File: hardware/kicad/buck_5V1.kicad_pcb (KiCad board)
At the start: 2 copper layers, 42.2 x 57.9 mm, 23 parts, among them J1 V12_IN, J2 V5_OUT, U1 LMZ23610TZ/NOPB

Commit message: docs: added pcb export - buck_5V1
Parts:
- moved J2 5.47 mm to (126.9, 96.4), turned to 180 degrees
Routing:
- net /PGND: track 13.6 -> 44.2 mm, vias 0 -> 11
- net /V12_IN: track 0.00 -> 1.27 mm
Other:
- board text added: "+"
- board text added: "-"
- board text added: "12V"
- board text added: "5V"

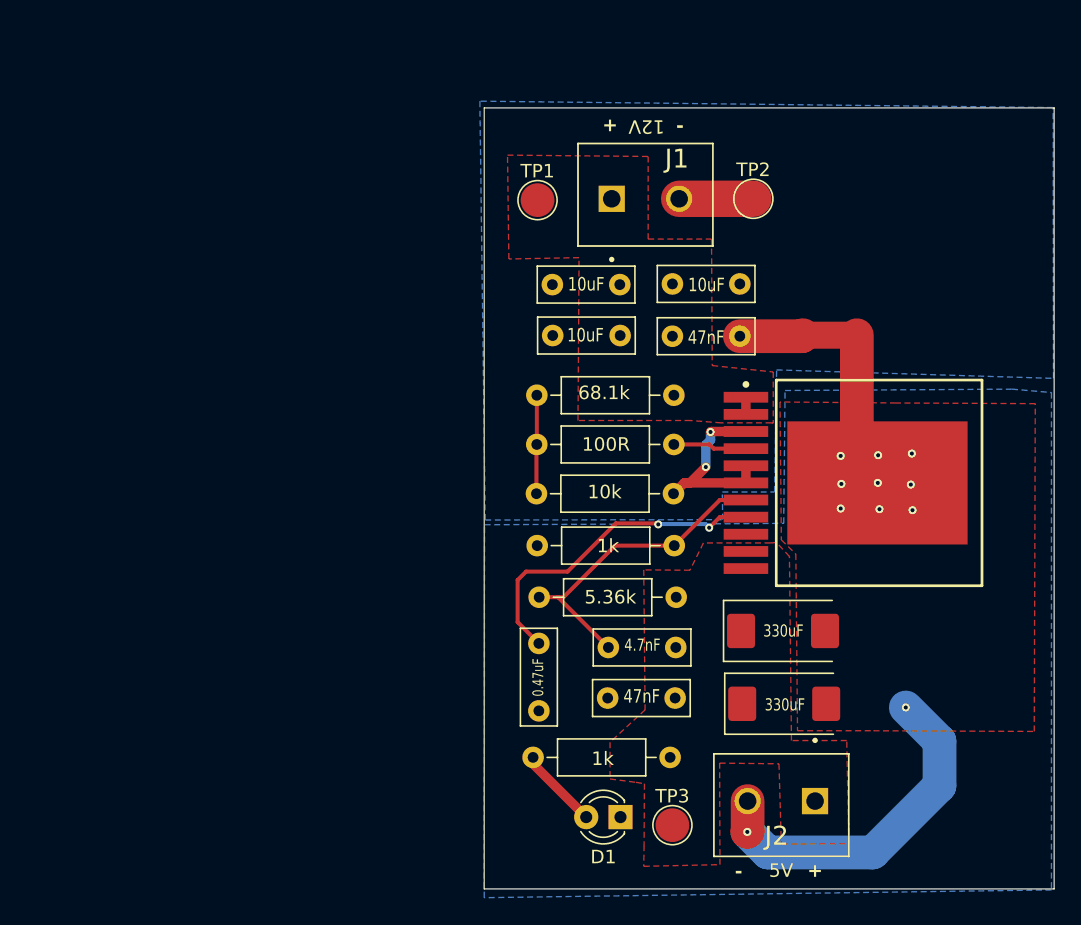
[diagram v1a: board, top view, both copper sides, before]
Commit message: fix: package change & pcb comp placement - buck5V1
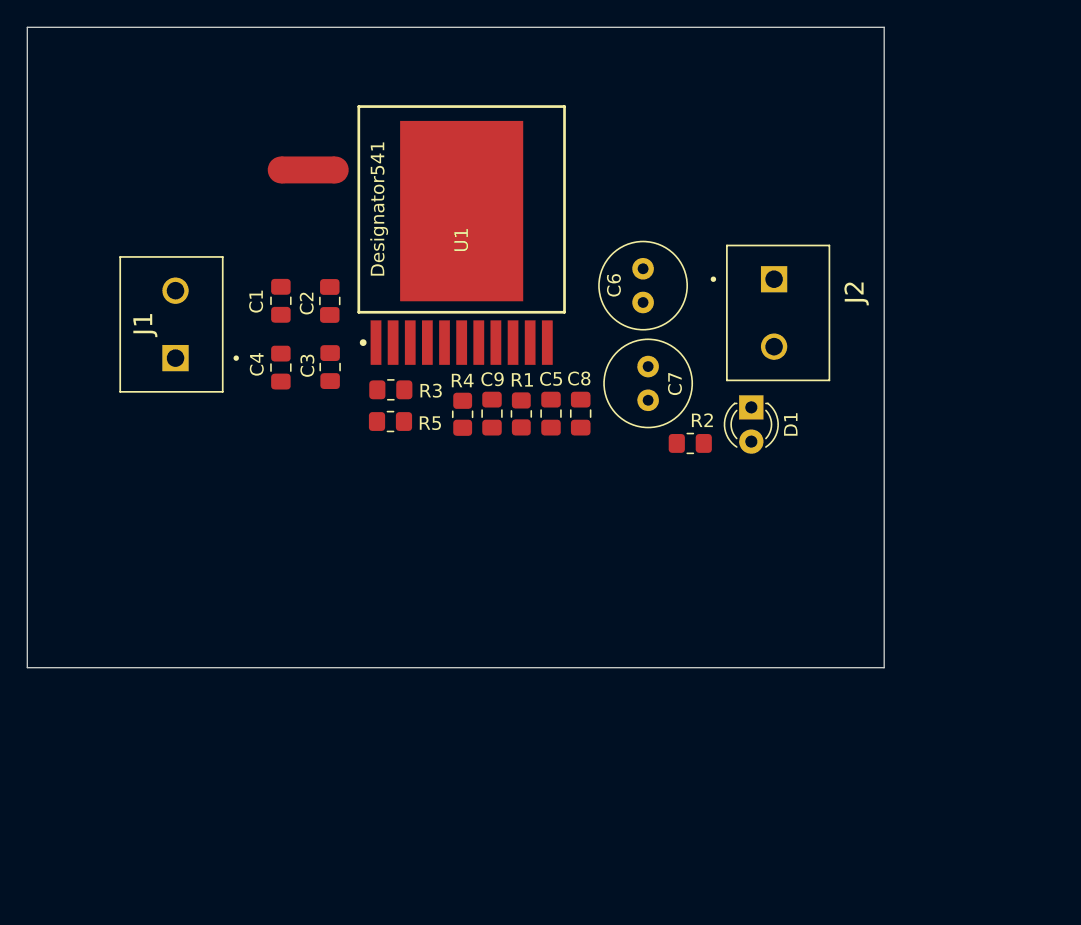
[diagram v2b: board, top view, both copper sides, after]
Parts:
- removed R6: 1k, Resistor_THT:R_Axial_DIN0207_L6.3mm_D2.5mm_P10.16mm_Horizontal
- removed TP1: V12_IN, TestPoint:TestPoint_Pad_D2.5mm
- removed TP2: GND, TestPoint:TestPoint_Pad_D2.5mm
- removed TP3: V5, TestPoint:TestPoint_Pad_D2.5mm
- C1, C2, C3, C5, C8: footprint Capacitor_THT:C_Disc_D7.0mm_W2.5mm_P5.00mm -> Capacitor_SMD:C_0805_2012Metric_Pad1.18x1.45mm_HandSolder
- C4: value 0.47uF -> 47nF; footprint Capacitor_THT:C_Disc_D7.0mm_W2.5mm_P5.00mm -> Capacitor_SMD:C_0805_2012Metric_Pad1.18x1.45mm_HandSolder
- C6, C7: footprint Capacitor_Tantalum_SMD:CP_EIA-7343-43_Kemet-X -> Capacitor_THT:C_Radial_D6.3mm_H5.0mm_P2.50mm
- C9: value 47nF -> 0.47uF; footprint Capacitor_THT:C_Disc_D7.0mm_W2.5mm_P5.00mm -> Capacitor_SMD:C_0805_2012Metric_Pad1.18x1.45mm_HandSolder
- R1: value 68.1k -> 5.36k; footprint Resistor_THT:R_Axial_DIN0207_L6.3mm_D2.5mm_P10.16mm_Horizontal -> Resistor_SMD:R_0805_2012Metric_Pad1.20x1.40mm_HandSolder
- R2: value 10k -> 1k; footprint Resistor_THT:R_Axial_DIN0207_L6.3mm_D2.5mm_P10.16mm_Horizontal -> Resistor_SMD:R_0805_2012Metric_Pad1.20x1.40mm_HandSolder
- R3: value 100R -> 68.1k; footprint Resistor_THT:R_Axial_DIN0207_L6.3mm_D2.5mm_P10.16mm_Horizontal -> Resistor_SMD:R_0805_2012Metric_Pad1.20x1.40mm_HandSolder
- R4: value 5.36k -> 1k; footprint Resistor_THT:R_Axial_DIN0207_L6.3mm_D2.5mm_P10.16mm_Horizontal -> Resistor_SMD:R_0805_2012Metric_Pad1.20x1.40mm_HandSolder
- R5: value 1k -> 10k; footprint Resistor_THT:R_Axial_DIN0207_L6.3mm_D2.5mm_P10.16mm_Horizontal -> Resistor_SMD:R_0805_2012Metric_Pad1.20x1.40mm_HandSolder
- moved NT1 40.6 mm to (89.3, 49.6)
- moved J2 38.8 mm to (123.8, 57.7), turned to -90 degrees
- moved J1 34.4 mm to (79.5, 63.6), turned to 90 degrees
- moved U1 33.9 mm to (100.7, 54.8), turned to 90 degrees
- moved D1 31.9 mm to (122.2, 67.2), turned to -90 degrees
- moved C6 31.5 mm to (114.1, 59.5), turned to 90 degrees
- moved C4 28.0 mm to (87.3, 64.3)
- moved C2 25.4 mm to (90.9, 59.3), turned to 90 degrees
- moved C1 25.2 mm to (87.3, 59.3), turned to 90 degrees
- moved C9 25.1 mm to (102.9, 67.7), turned to -90 degrees
- moved C7 22.0 mm to (114.5, 64.2), turned to -90 degrees
- moved C3 21.6 mm to (90.9, 64.2), turned to -90 degrees
- moved C5 19.7 mm to (107.3, 67.7), turned to 90 degrees
- moved R4 14.7 mm to (100.8, 67.7), turned to 90 degrees
- moved R5 14.2 mm to (95.4, 68.3)
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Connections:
- C4 pad 1: Net-(U1-SS) -> /V12_IN
- C4 pad 2: /PGND -> /AGND
- C8 pad 1: /V12_IN -> /V5_OUT
- C8 pad 2: /AGND -> /PGND
- C9 pad 1: /V5_OUT -> Net-(U1-SS)
- R1 pad 1: /V12_IN -> Net-(U1-FB)
- R1 pad 2: Net-(R1-Pad2) -> /V5_OUT
- R2 pad 1: /AGND -> Net-(D1-A)
- R2 pad 2: Net-(R1-Pad2) -> /V5_OUT
- R3 pad 1: Net-(R1-Pad2) -> /V12_IN
- R4 pad 1: Net-(U1-FB) -> /PGND
- R4 pad 2: /V5_OUT -> Net-(U1-FB)
- R5 pad 1: /PGND -> /AGND
- R5 pad 2: Net-(U1-FB) -> Net-(U1-EN)
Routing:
- net /PGND: track 44.2 -> 0.00 mm, vias 11 -> 0
- net /AGND: track 24.6 -> 0.00 mm, vias 2 -> 0
- net Net-(U1-SS): track 24.5 -> 0.00 mm, vias 2 -> 0
- net Net-(U1-FB): track 23.6 -> 0.00 mm
- net Net-(R1-Pad2): track 7.31 -> 0.00 mm
- net Net-(D1-A): track 6.06 -> 0.00 mm
- net Net-(U1-EN): track 5.47 -> 0.00 mm
- net /V12_IN: track 1.27 -> 0.00 mm
- removed copper zone on B.Cu, net /AGND
- removed copper zone on B.Cu, net /PGND
- removed copper zone on F.Cu, net /PGND
- removed copper zone on F.Cu, net /V12_IN
- removed copper zone on F.Cu, net /V5_OUT
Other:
- board size 42.2 x 57.9 mm -> 63.5 x 47.5 mm
- board text removed: "+"
- board text removed: "-"
- board text removed: "12V"
- board text removed: "5V"
